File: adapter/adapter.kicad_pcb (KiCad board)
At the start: 2 copper layers, 93.5 x 50.9 mm, 64 parts, among them J1 Serial, J10 Ribbon, J11 Ribbon, J12 Ribbon, J13 serial, J14 serial, J2 Serial, J3 battery charge, J4 RGB, J5 RGB, J6 battery charge, J7 trackball, J8 trackball, J9 Ribbon, SW1 SW_SPST, SW2 SW_SPST, SW3 SW_SPDT, SW4 SW_SPDT, U1 eliteC, U2 eliteC

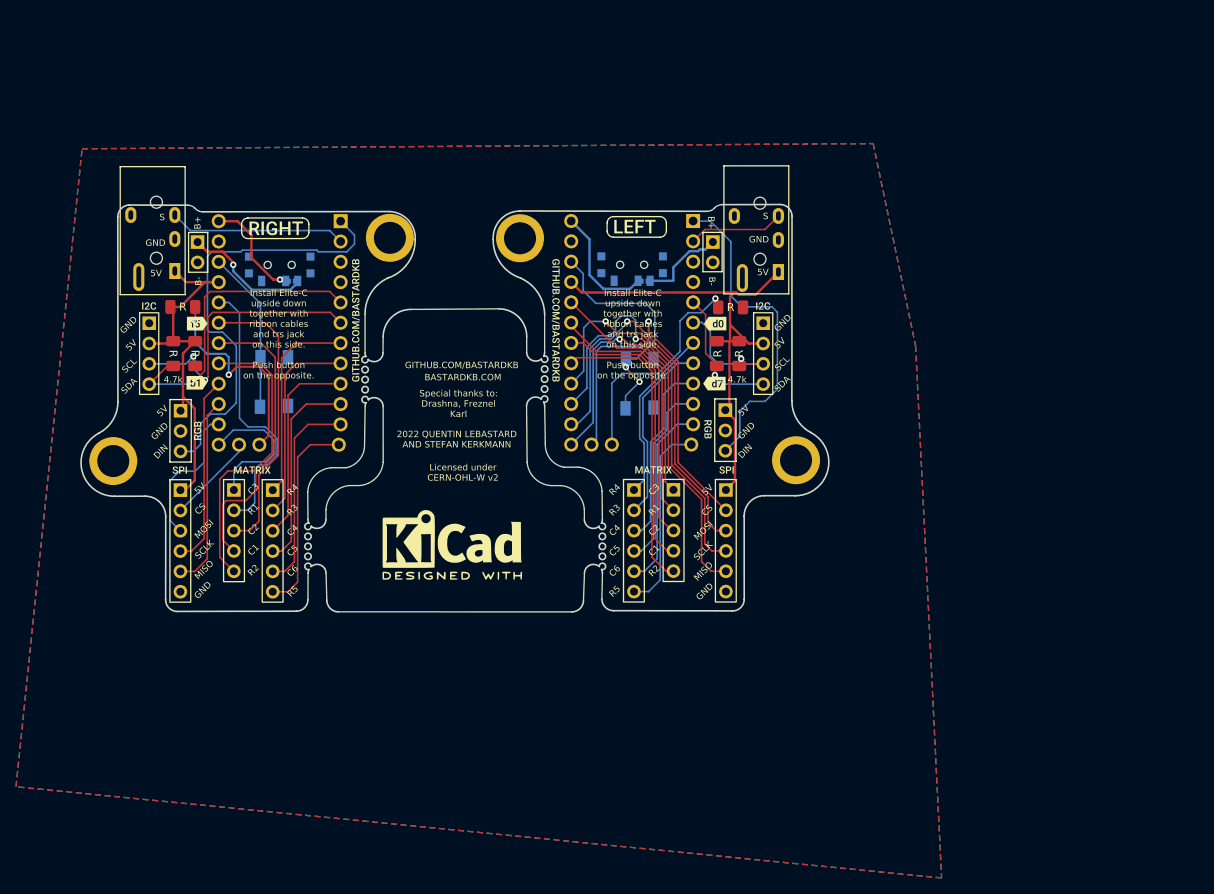
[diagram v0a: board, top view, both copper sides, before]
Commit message: initial work on rj9 mod
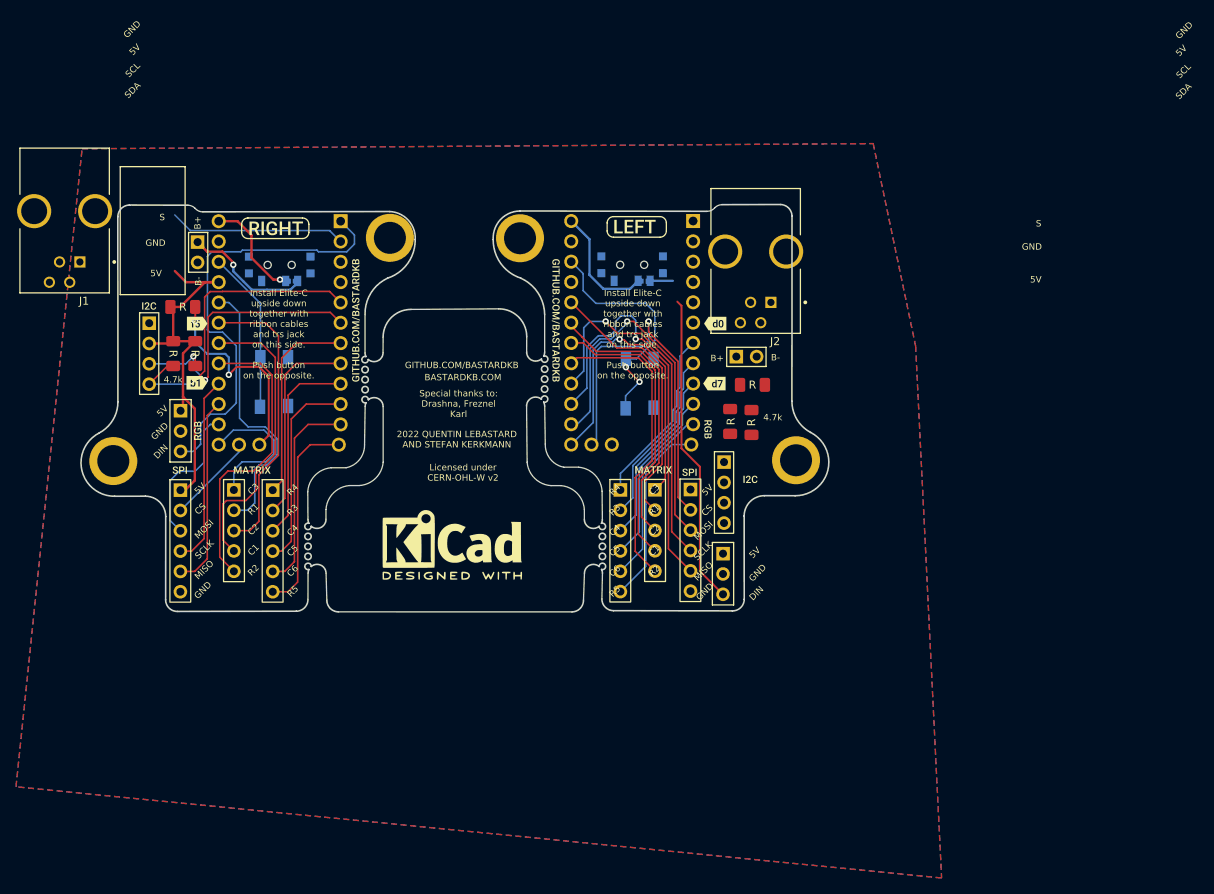
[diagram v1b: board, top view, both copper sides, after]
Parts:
- J1, J2: value Serial -> RJ9; footprint Library:Jack_3.5mm_PJ320E_Horizontal -> JohnDeereLibrary:MOLEX_0955012401; moved to F.Cu
- moved kibuzzard-620B8D91 21.7 mm to (192.4, 101.5) (x2)
- moved J13 18.0 mm to (189.1, 99.3)
- moved J5 17.9 mm to (189.0, 110.8)
- moved J1 15.7 mm to (106.7, 67.9)
- moved J6 14.6 mm to (190.6, 86.1), turned to 90 degrees
- moved R5 10.1 mm to (192.7, 89.7)
- moved R1 8.75 mm to (192.5, 94.4)
- moved R3 8.64 mm to (189.9, 94.2)
- moved kibuzzard-61F01957 4.65 mm to (184.8, 100.6)
- moved J8 4.43 mm to (184.9, 102.7)
- moved J2 3.82 mm to (193.1, 73.0)
- moved J11 2.31 mm to (180.5, 102.8)
- moved J12 1.70 mm to (176.1, 102.8)
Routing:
- net +5V: track 108.3 -> 46.5 mm
- net split_hand_r: track 28.5 -> 0.00 mm, vias 1 -> 0
- net scl_r: track 19.9 -> 0.04 mm, vias 1 -> 0
- net sda_r: track 16.9 -> 0.00 mm, vias 1 -> 0
- net serial_r: track 12.0 -> 0.00 mm
- net bat_sw_r: track 10.8 -> 2.83 mm
- net miso_r: track 54.1 -> 51.1 mm
- net sc_r: track 48.4 -> 45.4 mm
- net mosi_r: track 49.5 -> 46.9 mm
- net ss_r: track 49.0 -> 47.1 mm
- net rgb_l: track 40.4 -> 39.0 mm
- net col4_r: track 23.3 -> 22.1 mm
- net col5_r: track 23.3 -> 22.2 mm
- net row3_r: track 23.1 -> 22.1 mm
- net row1_r: track 33.1 -> 34.0 mm
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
